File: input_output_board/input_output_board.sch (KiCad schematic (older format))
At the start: 16 parts, among them J1 Neutrik_NCJ6FA-H, J2 Neutrik_NCJ6FA-H, J3 Neutrik_NCJ6FA-H, J4 Neutrik_NCJ6FA-H, J5 Molex_SL_01x04_Male, J6 Conn_02x08_Odd_Even, J7 Molex_SL_01x04_Male, J8 AudioJack3, K1 G6S-2, K2 G6S-2, K3 G6S-2, K4 G6S-2

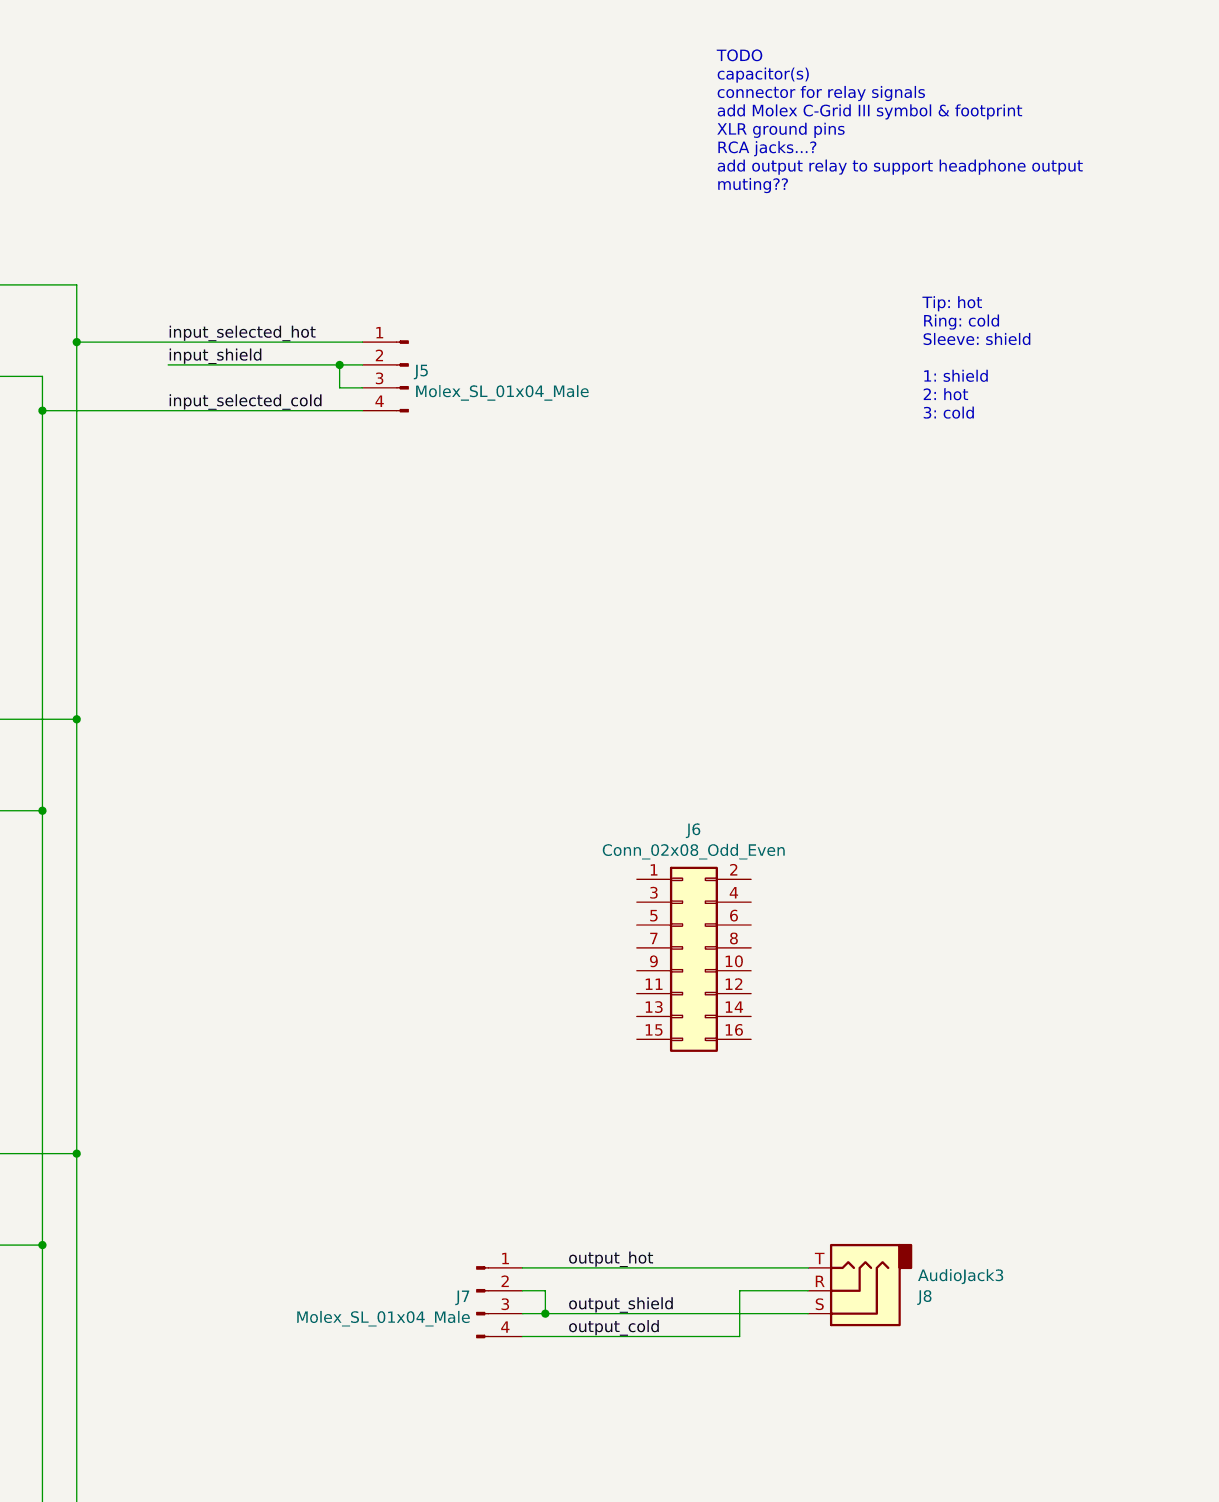
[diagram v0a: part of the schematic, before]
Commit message: add output relay
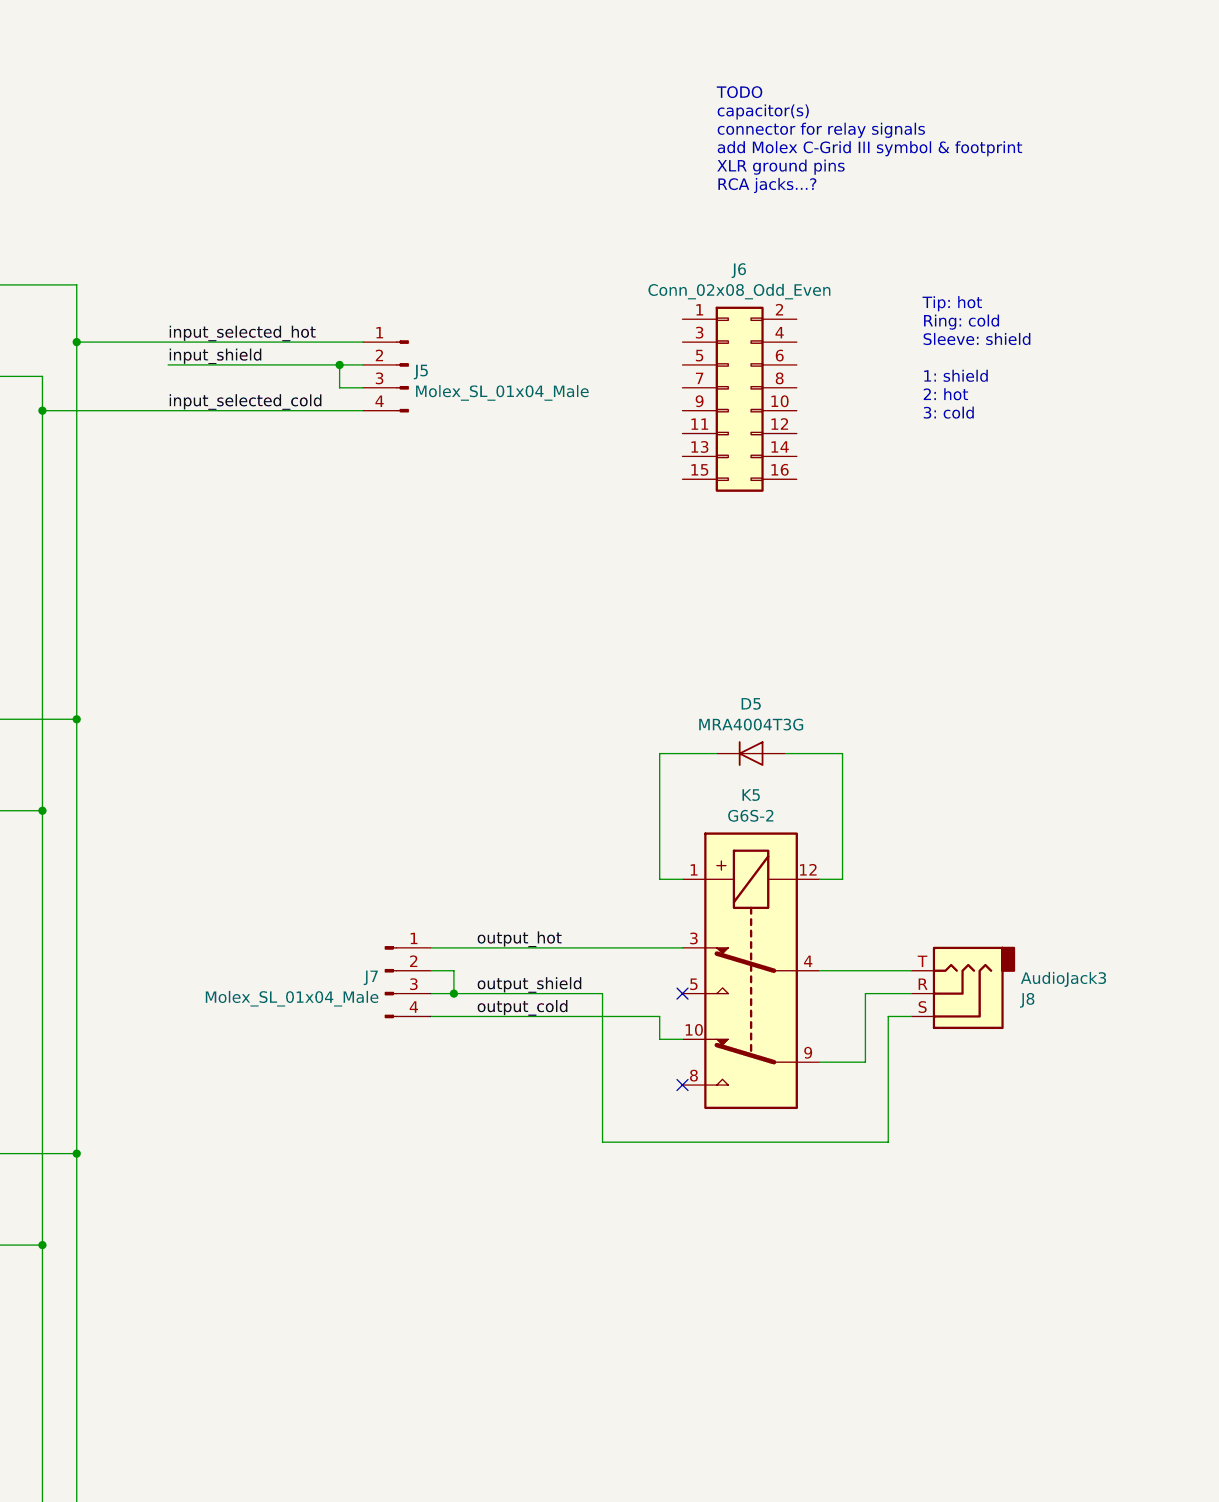
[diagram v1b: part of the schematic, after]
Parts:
- added D5: MRA4004T3G, Diode_SMD:D_SMA, symbol Device:D
- added K5: G6S-2, Relay_SMD:Relay_DPDT_Omron_G6S-2F, symbol Relay:G6S-2
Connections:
- net output_cold: now also K5.10; no longer J8.R
- net output_hot: now also K5.3; no longer J8.T
- new net: J8.R, K5.9
- new net: J8.T, K5.4
- new net: D5.1 (K), K5.1
- new net: D5.2 (A), K5.12
- no-connect marks 8 -> 10
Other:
- note added: "TODO\ncapacitor(s)\nconnector for relay signals\nadd Molex C-Grid III symbol & footprint\nXLR ground pins\nRCA jacks...?"
- note removed: "TODO\ncapacitor(s)\nconnector for relay signals\nadd Molex C-Grid III symbol & footprint\nXLR ground pins\nRCA jacks...?\nadd output relay to support headphone output\nmuting??"
- moved on the sheet: J6, J7, J8
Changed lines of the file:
@@
 L Connector:AudioJack3 J8
 U 1 1 5CAA8F23
-P 9300 6050
-F 0 "J8" H 9020 6075 50  0000 R CNN
-F 1 "AudioJack3" H 9020 5984 50  0000 R CNN
-F 2 "" H 9300 6050 50  0001 C CNN
-F 3 "~" H 9300 6050 50  0001 C CNN
-	1    9300 6050
+P 9750 4750
+F 0 "J8" H 9470 4775 50  0000 R CNN
+F 1 "AudioJack3" H 9470 4684 50  0000 R CNN
+F 2 "" H 9750 4750 50  0001 C CNN
+F 3 "~" H 9750 4750 50  0001 C CNN
+	1    9750 4750
 	-1   0    0    1
 $EndComp
@@
 L Connector_gkeeth:Molex_SL_01x04_Male J7
 U 1 1 5CB5BBEB
-P 7650 6050
-F 0 "J7" H 7623 6024 50  0000 R CNN
-F 1 "Molex_SL_01x04_Male" H 7623 5933 50  0000 R CNN
-F 2 "Connector_Molex_SL:Molex_SL_A-70543-0003_1x04_P2.54mm_Vertical" H 7650 6050 50  0001 C CNN
-F 3 "https://www.molex.com/pdm_docs/sd/705430001_sd.pdf" H 7650 6050 50  0001 C CNN
-	1    7650 6050
-	1    0    0    -1
-$EndComp
-Wire Wire Line
-	7850 5950 9100 5950
-Wire Wire Line
-	9100 6050 8800 6050
-Wire Wire Line
-	8800 6050 8800 6250
-Wire Wire Line
-	8800 6250 7850 6250
-Text Label 8050 5950 0    50   ~ 0
+P 7250 4650
+F 0 "J7" H 7223 4624 50  0000 R CNN
+F 1 "Molex_SL_01x04_Male" H 7223 4533 50  0000 R CNN
+F 2 "Connector_Molex_SL:Molex_SL_A-70543-0003_1x04_P2.54mm_Vertical" H 7250 4650 50  0001 C CNN
+F 3 "https://www.molex.com/pdm_docs/sd/705430001_sd.pdf" H 7250 4650 50  0001 C CNN
+	1    7250 4650
+	1    0    0    -1
+$EndComp
+Wire Wire Line
+	8450 4850 7450 4850
+Text Label 7650 4550 0    50   ~ 0
 output_hot
-Text Label 8050 6250 0    50   ~ 0
+Text Label 7650 4850 0    50   ~ 0
 output_cold
 Wire Wire Line
-	7850 6150 7950 6150
-Wire Wire Line
-	7850 6050 7950 6050
-Wire Wire Line
-	7950 6050 7950 6150
-Connection ~ 7950 6150
-Wire Wire Line
-	7950 6150 9100 6150
-Text Label 8050 6150 0    50   ~ 0
+	7450 4750 7550 4750
+Wire Wire Line
+	7450 4650 7550 4650
+Wire Wire Line
+	7550 4650 7550 4750
+Connection ~ 7550 4750
+Wire Wire Line
+	7550 4750 8200 4750
+Text Label 7650 4750 0    50   ~ 0
 output_shield
 Text Notes 8700 1250 0    50   ~ 0
-TODO\ncapacitor(s)\nconnector for relay signals\nadd Molex C-Grid III symbol & footprint\nXLR ground pins\nRCA jacks...?\nadd output relay to support headphone output\nmuting??
+TODO\ncapacitor(s)\nconnector for relay signals\nadd Molex C-Grid III symbol & footprint\nXLR ground pins\nRCA jacks...?
 $Comp
 L Connector_Generic:Conn_02x08_Odd_Even J6
 U 1 1 5CB676D4
-P 8550 4550
-F 0 "J6" H 8600 5067 50  0000 C CNN
-F 1 "Conn_02x08_Odd_Even" H 8600 4976 50  0000 C CNN
-F 2 "" H 8550 4550 50  0001 C CNN
-F 3 "~" H 8550 4550 50  0001 C CNN
-	1    8550 4550
+P 8750 2100
+F 0 "J6" H 8800 2617 50  0000 C CNN
+F 1 "Conn_02x08_Odd_Even" H 8800 2526 50  0000 C CNN
+F 2 "" H 8750 2100 50  0001 C CNN
+F 3 "~" H 8750 2100 50  0001 C CNN
+	1    8750 2100
 	1    0    0    -1
 $EndComp
@@
 NoConn ~ 4800 7250
 NoConn ~ 4800 7650
+$Comp
+L Relay:G6S-2 K5
+U 1 1 5CC507E9
+P 8850 4650
+F 0 "K5" V 8083 4650 50  0000 C CNN
+F 1 "G6S-2" V 8174 4650 50  0000 C CNN
+F 2 "Relay_SMD:Relay_DPDT_Omron_G6S-2F" H 9500 4600 50  0001 L CNN
+F 3 "http://omronfs.omron.com/en_US/ecb/products/pdf/en-g6s.pdf" H 8650 4650 50  0001 C CNN
+F 4 "Omron" H 8850 4650 50  0001 C CNN "Manufacturer"
+F 5 "G6S-2F DC12" H 8850 4650 50  0001 C CNN "Manufacturer PN"
+F 6 "Digikey" H 8850 4650 50  0001 C CNN "Distributor"
+F 7 "Z889-ND" H 8850 4650 50  0001 C CNN "Distributor PN"
+F 8 "https://www.digikey.com/product-detail/en/omron-electronics-inc-emc-div/G6S-2F-DC12/Z889-ND/27491" H 8850 4650 50  0001 C CNN "URL"
+F 9 "3.64" H 8850 4650 50  0001 C CNN "Unit Price"
+	1    8850 4650
+	0    -1   1    0
+$EndComp
+$Comp
+L Device:D D5
+U 1 1 5CC51A5E
+P 8850 3700
+F 0 "D5" H 8850 3916 50  0000 C CNN
+F 1 "MRA4004T3G" H 8850 3825 50  0000 C CNN
+F 2 "Diode_SMD:D_SMA" H 8850 3700 50  0001 C CNN
+F 3 "http://www.onsemi.com/pub_link/Collateral/MRA4003T3-D.PDF" H 8850 3700 50  0001 C CNN
+F 4 "On Semiconductor" H 8850 3700 50  0001 C CNN "Manufacturer"
+F 5 "MRA4004T3G" H 8850 3700 50  0001 C CNN "Manufacturer PN"
+F 6 "Digikey" H 8850 3700 50  0001 C CNN "Distributor"
+F 7 "MRA4004T3GOSCT-ND" H 8850 3700 50  0001 C CNN "Distributor PN"
+F 8 "https://www.digikey.com/products/en/discrete-semiconductor-products/diodes-rectifiers-single/280?k=MRA4004T3G&k=&pkeyword=MRA4004T3G&sv=0&pv7=2&sf=0&quantity=&ColumnSort=0&page=1&pageSize=25" H 8850 3700 50  0001 C CNN "URL"
+F 9 "0.29" H 8850 3700 50  0001 C CNN "Unit Price"
+	1    8850 3700
+	1    0    0    -1
+$EndComp
+Wire Wire Line
+	9550 4650 9150 4650
+Wire Wire Line
+	9150 5050 9350 5050
+Wire Wire Line
+	9350 5050 9350 4750
+Wire Wire Line
+	9350 4750 9550 4750
+Wire Wire Line
+	8450 4850 8450 4950
+Wire Wire Line
+	8450 4950 8550 4950
+Wire Wire Line
+	7450 4550 8550 4550
+Wire Wire Line
+	8200 4750 8200 5400
+Wire Wire Line
+	8200 5400 9450 5400
+Wire Wire Line
+	9450 5400 9450 4850
+Wire Wire Line
+	9450 4850 9550 4850
+Wire Wire Line
+	8700 3700 8450 3700
+Wire Wire Line
+	8450 3700 8450 4250
+Wire Wire Line
+	8450 4250 8550 4250
+Wire Wire Line
+	9150 4250 9250 4250
+Wire Wire Line
+	9250 4250 9250 3700
+Wire Wire Line
+	9250 3700 9000 3700
+NoConn ~ 8550 5150
+NoConn ~ 8550 4750
 $EndSCHEMATC
